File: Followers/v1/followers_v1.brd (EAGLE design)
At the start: 19 x 108.4 mm, 93 parts, among them IC1 OPA1641, IC2 LM324PW, IC3 LM324PW, IC4 TL072D, IC6 LM4040B10, IC9 LM324PW, J1 PJ301_THONKICONN6, J10 PJ301_THONKICONN6, J11 PJ301_THONKICONN6, J2 PJ301_THONKICONN6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

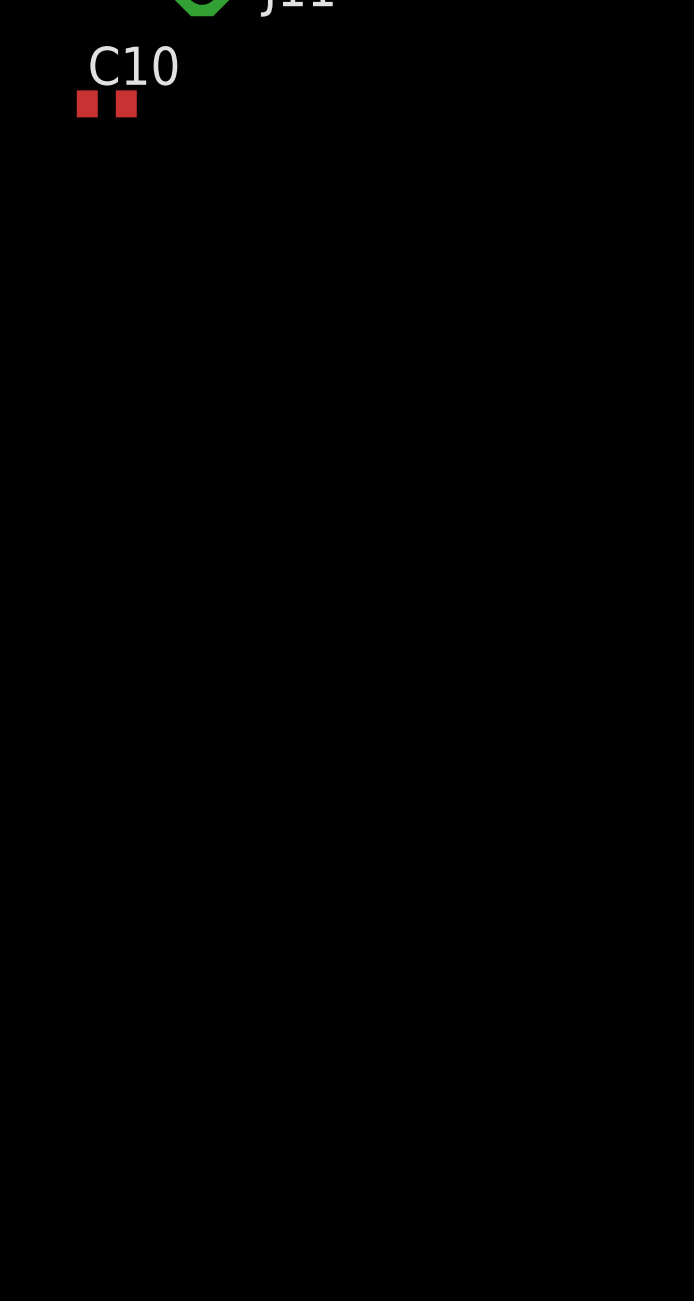
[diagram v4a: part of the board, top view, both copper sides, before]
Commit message: Input resistor
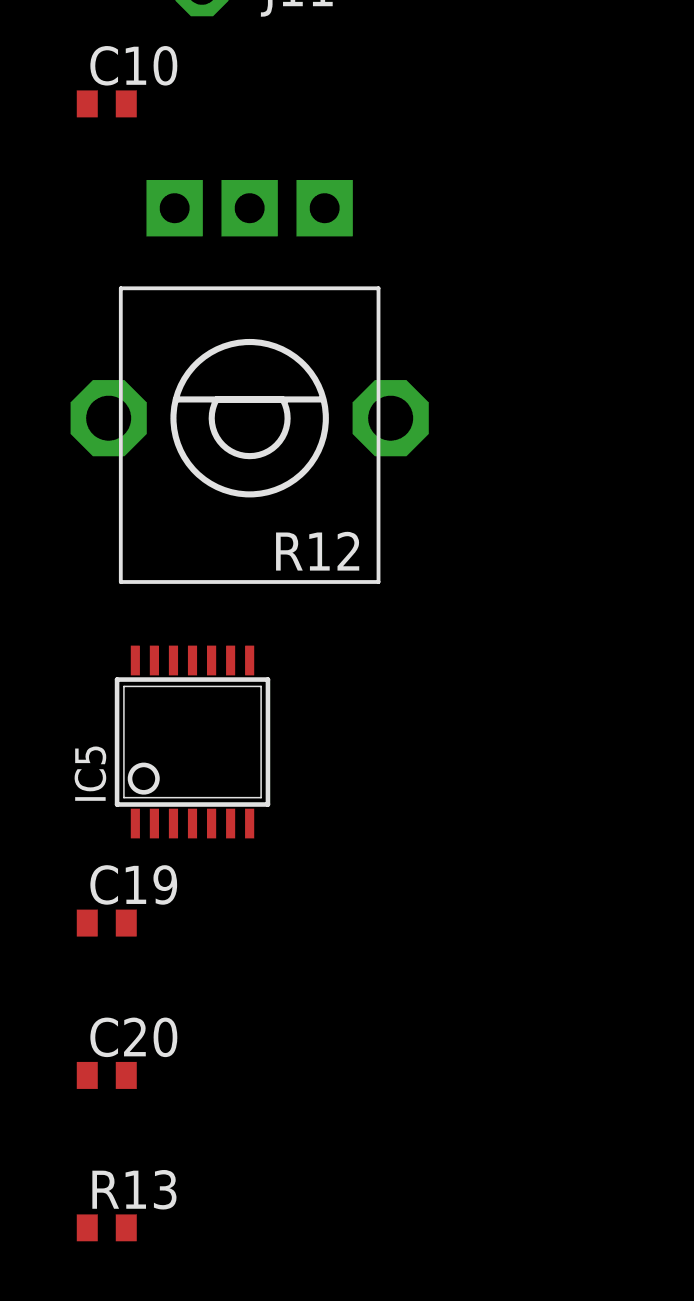
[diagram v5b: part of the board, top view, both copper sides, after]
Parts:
- added C19, C20: 100n, rcl:C0402
- added IC5: LM324PW, og-ics:TSSOP14
- added R12: 50k, og-pots:ALPS_POT_VERTICAL_PS
- added R13: 1k, rcl:R0402
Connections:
- new net N$1: J7.P3, R13.1
- new net N$8: IC5.1, IC5.2, R25.1
- net GND: now also C19.2, C20.1
- net N$29: now also IC5.3, R13.2; no longer J7.P3, R25.1
- net VCC: now also C19.1, IC5.4
- net VEE: now also C20.2, IC5.11
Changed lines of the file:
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@@
 <attribute name="VALUE" x="0" y="-381.3175" size="1.27" layer="27"/>
+</element>
+<element name="R12" library="og-pots" package="ALPS_POT_VERTICAL_PS" value="50k" x="5.3975" y="-389.89" smashed="yes">
+<attribute name="NAME" x="9.2075" y="-393.7" size="1.27" layer="25" rot="R180"/>
+<attribute name="VALUE" x="9.2075" y="-392.176" size="1.27" layer="27" rot="R180"/>
+</element>
+<element name="IC5" library="og-ics" package="TSSOP14" value="LM324PW" x="3.4925" y="-400.685" smashed="yes">
+<attribute name="NAME" x="0.5969" y="-402.7678" size="1.016" layer="25" ratio="10" rot="R90"/>
+<attribute name="VALUE" x="7.3787" y="-402.7678" size="1.016" layer="27" ratio="10" rot="R90"/>
+</element>
+<element name="C19" library="rcl" package="C0402" value="100n" x="0.635" y="-406.7175" smashed="yes">
+<attribute name="NAME" x="0" y="-406.0825" size="1.27" layer="25"/>
+<attribute name="VALUE" x="0" y="-408.6225" size="1.27" layer="27"/>
+</element>
+<element name="C20" library="rcl" package="C0402" value="100n" x="0.635" y="-411.7975" smashed="yes">
+<attribute name="NAME" x="0" y="-411.1625" size="1.27" layer="25"/>
+<attribute name="VALUE" x="0" y="-413.7025" size="1.27" layer="27"/>
+</element>
+<element name="R13" library="rcl" package="R0402" value="1k" x="0.635" y="-416.8775" smashed="yes">
+<attribute name="NAME" x="0" y="-416.2425" size="1.27" layer="25"/>
+<attribute name="VALUE" x="0" y="-418.7825" size="1.27" layer="27"/>
 </element>
 </elements>
@@
 <contactref element="J4" pad="P1"/>
 <contactref element="J11" pad="P1"/>
+<contactref element="C19" pad="2"/>
+<contactref element="C20" pad="1"/>
 <wire x1="4.7475" y1="-270.1925" x2="1.285" y2="-241.935" width="0" layer="19" extent="1-1"/>
 <wire x1="3.305" y1="-280.3525" x2="4.7475" y2="-270.1925" width="0" layer="19" extent="1-1"/>
@@
 <wire x1="3.81" y1="-357.505" x2="3.81" y2="-344.4875" width="0" layer="19" extent="1-1"/>
 <wire x1="3.81" y1="-375.6025" x2="3.81" y2="-357.505" width="0" layer="19" extent="1-1"/>
+<wire x1="1.285" y1="-406.7175" x2="3.81" y2="-375.6025" width="0" layer="19" extent="1-1"/>
+<wire x1="-0.015" y1="-411.7975" x2="1.285" y2="-406.7175" width="0" layer="19" extent="1-1"/>
 <wire x1="1.8025" y1="-199.39" x2="1.285" y2="-241.935" width="0" layer="19" extent="1-1"/>
 <wire x1="2.855" y1="-194.14" x2="1.8025" y2="-199.39" width="0" layer="19" extent="1-1"/>
@@
 <contactref element="IC2" pad="11"/>
 <contactref element="C18" pad="2"/>
-<wire x1="12.3975" y1="72.7075" x2="17.6212" y2="105.3037" width="0" layer="19" extent="1-1"/>
-<wire x1="8.7125" y1="69.51" x2="12.3975" y2="72.7075" width="0" layer="19" extent="1-1"/>
-<wire x1="13.8303" y1="34.925" x2="8.7125" y2="69.51" width="0" layer="19" extent="1-1"/>
-<wire x1="10.4625" y1="15.5575" x2="13.8303" y2="34.925" width="0" layer="19" extent="1-1"/>
-<wire x1="12.2428" y1="12.065" x2="10.4625" y2="15.5575" width="0" layer="19" extent="1-1"/>
-<wire x1="3.305" y1="-286.7025" x2="12.2428" y2="12.065" width="0" layer="19" extent="1-1"/>
-<wire x1="1.285" y1="-302.5775" x2="3.305" y2="-286.7025" width="0" layer="19" extent="1-1"/>
+<contactref element="IC5" pad="11"/>
+<contactref element="C20" pad="2"/>
+<wire x1="3.4925" y1="-397.9672" x2="1.285" y2="-411.7975" width="0" layer="19" extent="1-1"/>
+<wire x1="1.285" y1="-302.5775" x2="3.4925" y2="-397.9672" width="0" layer="19" extent="1-1"/>
+<wire x1="3.305" y1="-286.7025" x2="1.285" y2="-302.5775" width="0" layer="19" extent="1-1"/>
+<wire x1="12.2428" y1="12.065" x2="3.305" y2="-286.7025" width="0" layer="19" extent="1-1"/>
+<wire x1="10.4625" y1="15.5575" x2="12.2428" y2="12.065" width="0" layer="19" extent="1-1"/>
+<wire x1="13.8303" y1="34.925" x2="10.4625" y2="15.5575" width="0" layer="19" extent="1-1"/>
+<wire x1="8.7125" y1="69.51" x2="13.8303" y2="34.925" width="0" layer="19" extent="1-1"/>
+<wire x1="12.3975" y1="72.7075" x2="8.7125" y2="69.51" width="0" layer="19" extent="1-1"/>
+<wire x1="17.6212" y1="105.3037" x2="12.3975" y2="72.7075" width="0" layer="19" extent="1-1"/>
 </signal>
 <signal name="VCC">
@@
 <contactref element="IC2" pad="4"/>
 <contactref element="C9" pad="1"/>
+<contactref element="IC5" pad="4"/>
+<contactref element="C19" pad="1"/>
 <wire x1="11.215" y1="-182.245" x2="5.5" y2="-199.39" width="0" layer="19" extent="1-1"/>
 <wire x1="7.5175" y1="-172.085" x2="11.215" y2="-182.245" width="0" layer="19" extent="1-1"/>
@@
 <wire x1="0.505" y1="-280.3525" x2="5.5" y2="-199.39" width="0" layer="19" extent="1-1"/>
 <wire x1="-0.015" y1="-297.4975" x2="0.505" y2="-280.3525" width="0" layer="19" extent="1-1"/>
+<wire x1="3.4925" y1="-403.4028" x2="-0.015" y2="-297.4975" width="0" layer="19" extent="1-1"/>
+<wire x1="-0.015" y1="-406.7175" x2="3.4925" y2="-403.4028" width="0" layer="19" extent="1-1"/>
 <wire x1="6.8072" y1="12.065" x2="1.905" y2="-157.42" width="0" layer="19" extent="1-1"/>
 <wire x1="5.3975" y1="13.32" x2="6.8072" y2="12.065" width="0" layer="19" extent="1-1"/>
@@
 <wire x1="9.54" y1="-11.43" x2="8.3947" y2="34.29" width="0" layer="19" extent="1-1"/>
 </signal>
-<signal name="N$29">
-<contactref element="J7" pad="P3"/>
-<contactref element="R25" pad="1"/>
-<wire x1="3.81" y1="-63.1825" x2="11.0975" y2="-223.2025" width="0" layer="19" extent="1-1"/>
-</signal>
 <signal name="N$16">
 <contactref element="R2" pad="2"/>
@@
 <contactref element="J10" pad="P3"/>
 </signal>
+<signal name="N$8">
+<contactref element="IC5" pad="2"/>
+<contactref element="IC5" pad="1"/>
+<contactref element="R25" pad="1"/>
+<wire x1="2.2225" y1="-403.4028" x2="11.0975" y2="-223.2025" width="0" layer="19" extent="1-1"/>
+<wire x1="1.5875" y1="-403.4028" x2="2.2225" y2="-403.4028" width="0" layer="19" extent="1-1"/>
+</signal>
+<signal name="N$1">
+<contactref element="J7" pad="P3"/>
+<contactref element="R13" pad="1"/>
+<wire x1="3.81" y1="-63.1825" x2="-0.015" y2="-416.8775" width="0" layer="19" extent="1-1"/>
+</signal>
+<signal name="N$29">
+<contactref element="R13" pad="2"/>
+<contactref element="IC5" pad="3"/>
+<wire x1="2.8575" y1="-403.4028" x2="1.285" y2="-416.8775" width="0" layer="19" extent="1-1"/>
+</signal>
 </signals>

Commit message: Filter
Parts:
- removed IC9: LM324PW, og-ics:TSSOP14
- added C21: TBD, rcl:C0402
- added R14, R15, R16: 1k, rcl:R0402
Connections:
- removed net LP_DC: J11.P2, R23.1
- removed net V+: IC9.4
- removed net V-: IC9.11
- new net LOWPASS: IC5.8, IC5.9, J11.P2, R23.1
- new net N$35: C21.1, IC5.10, R12.P$3
- new net N$36: IC5.5, R14.2
- new net N$39: J8.P3, R14.1
- new net N$43: IC5.6, IC5.7, R12.P$2
- new net N$45: R16.2
- net COMP: now also IC5.12; no longer IC9.12
- net GND: now also C21.2
- net N$17: now also IC5.2; no longer IC3.13
- net N$29: now also IC3.12; no longer IC5.3
- net N$30: now also IC5.1; no longer IC3.14
- net N$37: now also IC5.13; no longer IC9.13
- net N$38: now also IC5.14; no longer IC9.14
- net N$41: now also R15.1
- net N$42: now also R16.1
- net N$8: now also IC3.13, IC3.14; no longer IC5.1, IC5.2
- net SLEW: now also IC5.3; no longer IC3.12
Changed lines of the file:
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@@
 <attribute name="VALUE" x="3.175" y="-248.3485" size="1.27" layer="27" ratio="10"/>
-</element>
-<element name="IC9" library="og-ics" package="TSSOP14" value="LM324PW" x="3.4925" y="-254" smashed="yes">
-<attribute name="NAME" x="0.5969" y="-256.0828" size="1.016" layer="25" ratio="10" rot="R90"/>
-<attribute name="VALUE" x="7.3787" y="-256.0828" size="1.016" layer="27" ratio="10" rot="R90"/>
 </element>
 <element name="LED3" library="led" package="LED3MM" value="WP710A10SEC/J4" x="1.27" y="-274.955" smashed="yes">
@@
 <attribute name="NAME" x="0" y="-416.2425" size="1.27" layer="25"/>
 <attribute name="VALUE" x="0" y="-418.7825" size="1.27" layer="27"/>
+</element>
+<element name="C21" library="rcl" package="C0402" value="TBD" x="0.635" y="-421.9575" smashed="yes">
+<attribute name="NAME" x="0" y="-421.3225" size="1.27" layer="25"/>
+<attribute name="VALUE" x="0" y="-423.8625" size="1.27" layer="27"/>
+</element>
+<element name="R14" library="rcl" package="R0402" value="1k" x="0.635" y="-427.0375" smashed="yes">
+<attribute name="NAME" x="0" y="-426.4025" size="1.27" layer="25"/>
+<attribute name="VALUE" x="0" y="-428.9425" size="1.27" layer="27"/>
+</element>
+<element name="R15" library="rcl" package="R0402" value="1k" x="0.635" y="-432.1175" smashed="yes">
+<attribute name="NAME" x="0" y="-431.4825" size="1.27" layer="25"/>
+<attribute name="VALUE" x="0" y="-434.0225" size="1.27" layer="27"/>
+</element>
+<element name="R16" library="rcl" package="R0402" value="1k" x="0.635" y="-437.1975" smashed="yes">
+<attribute name="NAME" x="0" y="-436.5625" size="1.27" layer="25"/>
+<attribute name="VALUE" x="0" y="-439.1025" size="1.27" layer="27"/>
 </element>
 </elements>
@@
 <contactref element="C19" pad="2"/>
 <contactref element="C20" pad="1"/>
+<contactref element="C21" pad="2"/>
 <wire x1="4.7475" y1="-270.1925" x2="1.285" y2="-241.935" width="0" layer="19" extent="1-1"/>
 <wire x1="3.305" y1="-280.3525" x2="4.7475" y2="-270.1925" width="0" layer="19" extent="1-1"/>
@@
 <wire x1="1.285" y1="-406.7175" x2="3.81" y2="-375.6025" width="0" layer="19" extent="1-1"/>
 <wire x1="-0.015" y1="-411.7975" x2="1.285" y2="-406.7175" width="0" layer="19" extent="1-1"/>
+<wire x1="1.285" y1="-421.9575" x2="-0.015" y2="-411.7975" width="0" layer="19" extent="1-1"/>
 <wire x1="1.8025" y1="-199.39" x2="1.285" y2="-241.935" width="0" layer="19" extent="1-1"/>
 <wire x1="2.855" y1="-194.14" x2="1.8025" y2="-199.39" width="0" layer="19" extent="1-1"/>
@@
 <wire x1="15.69" y1="67.31" x2="14.9225" y2="71.97" width="0" layer="19" extent="1-1"/>
 </signal>
-<signal name="V+">
-<contactref element="IC9" pad="4"/>
-</signal>
-<signal name="V-">
-<contactref element="IC9" pad="11"/>
-</signal>
 <signal name="N$7">
 <contactref element="R36" pad="2"/>
@@
 </signal>
 <signal name="SLEW">
-<contactref element="IC3" pad="12"/>
 <contactref element="C11" pad="2"/>
 <contactref element="R28" pad="2"/>
@@
 <contactref element="IC3" pad="8"/>
 <contactref element="J8" pad="P2"/>
+<contactref element="IC5" pad="3"/>
 <wire x1="1.6025" y1="-223.2025" x2="6.365" y2="-228.2825" width="0" layer="19" extent="1-1"/>
 <wire x1="3.81" y1="-341.9475" x2="6.365" y2="-228.2825" width="0" layer="19" extent="1-1"/>
+<wire x1="2.8575" y1="-403.4028" x2="3.81" y2="-341.9475" width="0" layer="19" extent="1-1"/>
 <wire x1="0.3025" y1="-90.17" x2="1.6025" y2="-223.2025" width="0" layer="19" extent="1-1"/>
 <wire x1="12.2428" y1="10.16" x2="0.3025" y2="-90.17" width="0" layer="19" extent="1-1"/>
-<wire x1="12.2428" y1="12.7" x2="12.2428" y2="10.16" width="0" layer="19" extent="1-1"/>
 </signal>
 <signal name="THRESH">
@@
 <signal name="COMP">
 <contactref element="R33" pad="1"/>
-<contactref element="IC9" pad="12"/>
-<wire x1="9.8275" y1="-108.2675" x2="2.8575" y2="-251.2822" width="0" layer="19" extent="1-1"/>
+<contactref element="IC5" pad="12"/>
+<wire x1="9.8275" y1="-108.2675" x2="2.8575" y2="-397.9672" width="0" layer="19" extent="1-1"/>
 </signal>
 <signal name="N$28">
@@
 <signal name="N$30">
 <contactref element="LED2" pad="A"/>
-<contactref element="IC3" pad="14"/>
-<wire x1="12.2428" y1="13.97" x2="0" y2="-246.6975" width="0" layer="19" extent="1-1"/>
+<contactref element="IC5" pad="1"/>
+<wire x1="1.5875" y1="-403.4028" x2="0" y2="-246.6975" width="0" layer="19" extent="1-1"/>
 </signal>
 <signal name="N$17">
 <contactref element="R9" pad="1"/>
 <contactref element="LED2" pad="K"/>
-<contactref element="IC3" pad="13"/>
+<contactref element="IC5" pad="2"/>
 <wire x1="-0.015" y1="-241.935" x2="2.54" y2="-246.6975" width="0" layer="19" extent="1-1"/>
-<wire x1="12.2428" y1="13.335" x2="-0.015" y2="-241.935" width="0" layer="19" extent="1-1"/>
+<wire x1="2.2225" y1="-403.4028" x2="2.54" y2="-246.6975" width="0" layer="19" extent="1-1"/>
 </signal>
 <signal name="N$37">
 <contactref element="LED3" pad="K"/>
-<contactref element="IC9" pad="13"/>
 <contactref element="R10" pad="2"/>
-<wire x1="6.0475" y1="-270.1925" x2="2.2225" y2="-251.2822" width="0" layer="19" extent="1-1"/>
-<wire x1="2.54" y1="-274.955" x2="6.0475" y2="-270.1925" width="0" layer="19" extent="1-1"/>
+<contactref element="IC5" pad="13"/>
+<wire x1="2.54" y1="-274.955" x2="2.2225" y2="-397.9672" width="0" layer="19" extent="1-1"/>
+<wire x1="6.0475" y1="-270.1925" x2="2.54" y2="-274.955" width="0" layer="19" extent="1-1"/>
 </signal>
 <signal name="N$38">
 <contactref element="LED3" pad="A"/>
-<contactref element="IC9" pad="14"/>
-<wire x1="0" y1="-274.955" x2="1.5875" y2="-251.2822" width="0" layer="19" extent="1-1"/>
+<contactref element="IC5" pad="14"/>
+<wire x1="0" y1="-274.955" x2="1.5875" y2="-397.9672" width="0" layer="19" extent="1-1"/>
 </signal>
 <signal name="N$27">
@@
 <wire x1="3.81" y1="-347.345" x2="1.285" y2="-361.315" width="0" layer="19" extent="1-1"/>
 </signal>
-<signal name="LP_DC">
+<signal name="LOWPASS">
 <contactref element="R23" pad="1"/>
 <contactref element="J11" pad="P2"/>
+<contactref element="IC5" pad="9"/>
+<contactref element="IC5" pad="8"/>
+<wire x1="5.3975" y1="-397.9672" x2="4.7625" y2="-397.9672" width="0" layer="19" extent="1-1"/>
+<wire x1="3.81" y1="-373.0625" x2="4.7625" y2="-397.9672" width="0" layer="19" extent="1-1"/>
 <wire x1="-0.015" y1="-361.315" x2="3.81" y2="-373.0625" width="0" layer="19" extent="1-1"/>
 </signal>
 <signal name="N$41">
 <contactref element="J11" pad="P3"/>
+<contactref element="R15" pad="1"/>
+<wire x1="3.81" y1="-365.4425" x2="-0.015" y2="-432.1175" width="0" layer="19" extent="1-1"/>
 </signal>
 <signal name="N$42">
 <contactref element="J10" pad="P3"/>
+<contactref element="R16" pad="1"/>
+<wire x1="3.81" y1="-120.3325" x2="-0.015" y2="-437.1975" width="0" layer="19" extent="1-1"/>
 </signal>
 <signal name="N$8">
-<contactref element="IC5" pad="2"/>
-<contactref element="IC5" pad="1"/>
 <contactref element="R25" pad="1"/>
-<wire x1="2.2225" y1="-403.4028" x2="11.0975" y2="-223.2025" width="0" layer="19" extent="1-1"/>
-<wire x1="1.5875" y1="-403.4028" x2="2.2225" y2="-403.4028" width="0" layer="19" extent="1-1"/>
+<contactref element="IC3" pad="14"/>
+<contactref element="IC3" pad="13"/>
+<wire x1="12.2428" y1="13.335" x2="11.0975" y2="-223.2025" width="0" layer="19" extent="1-1"/>
+<wire x1="12.2428" y1="13.97" x2="12.2428" y2="13.335" width="0" layer="19" extent="1-1"/>
 </signal>
 <signal name="N$1">
@@
 <signal name="N$29">
 <contactref element="R13" pad="2"/>
-<contactref element="IC5" pad="3"/>
-<wire x1="2.8575" y1="-403.4028" x2="1.285" y2="-416.8775" width="0" layer="19" extent="1-1"/>
+<contactref element="IC3" pad="12"/>
+<wire x1="12.2428" y1="12.7" x2="1.285" y2="-416.8775" width="0" layer="19" extent="1-1"/>
+</signal>
+<signal name="N$35">
+<contactref element="C21" pad="1"/>
+<contactref element="R12" pad="P$3"/>
+<contactref element="IC5" pad="10"/>
+<wire x1="4.1275" y1="-397.9672" x2="-0.015" y2="-421.9575" width="0" layer="19" extent="1-1"/>
+<wire x1="7.8975" y1="-382.89" x2="4.1275" y2="-397.9672" width="0" layer="19" extent="1-1"/>
+</signal>
+<signal name="N$36">
+<contactref element="IC5" pad="5"/>
+<contactref element="R14" pad="2"/>
+<wire x1="4.1275" y1="-403.4028" x2="1.285" y2="-427.0375" width="0" layer="19" extent="1-1"/>
+</signal>
+<signal name="N$39">
+<contactref element="R14" pad="1"/>
+<contactref element="J8" pad="P3"/>
+<wire x1="3.81" y1="-334.3275" x2="-0.015" y2="-427.0375" width="0" layer="19" extent="1-1"/>
+</signal>
+<signal name="N$43">
+<contactref element="IC5" pad="6"/>
+<contactref element="IC5" pad="7"/>
+<contactref element="R12" pad="P$2"/>
+<wire x1="5.3975" y1="-403.4028" x2="4.7625" y2="-403.4028" width="0" layer="19" extent="1-1"/>
+<wire x1="5.3975" y1="-382.89" x2="4.7625" y2="-403.4028" width="0" layer="19" extent="1-1"/>
+</signal>
+<signal name="N$45">
+<contactref element="R16" pad="2"/>
 </signal>
 </signals>
